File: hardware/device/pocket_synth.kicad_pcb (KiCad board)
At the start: 6 copper layers, 74 x 138 mm, 128 parts, among them IC2 IS42S16160J-7BLI, J1 POT_CONN, J10 HP_OUT, J2 USB, J3 MICRO_SD, J4 EXPANSION, J5 AUDIO_EXP, J8 LINE_OUT, J9 LINE_IN, SW1 TRIG1, SW10 TRIG10, SW11 TRIG11, SW12 TRIG12, SW13 TRIG13, SW14 TRIG14, SW15 TRIG15, SW16 TRIG16, SW17 KMR221NGLFS, SW18 HELP, SW2 TRIG2, SW3 TRIG3, SW4 TRIG4, SW5 TRIG5, SW6 TRIG6, SW7 TRIG7, SW8 TRIG8, SW9 TRIG9, U1 FSA2466UMX, U10 TRIG9, U11 TRIG13, U12 TRIG10, U13 TRIG14, U14 TRIG11, U15 TRIG15, U16 TRIG12, U17 TRIG16, U18 STM32H743ZIT6, U19 ER-TFT024IPS-3, U2 TRIG1, U20 TPS62A02DRL, U21 TPS560200, U22 MAX17261xxTD, U23 BQ21040DBV, U25 TCA8418RTWR, U26 FUSB303BTMX, U27 FUSB302B01MPX, U29 NAU88C22YG, U3 TRIG2, U4 TRIG3, U5 TRIG4, U6 TRIG8, U7 TRIG7, U8 TRIG6, U9 TRIG5

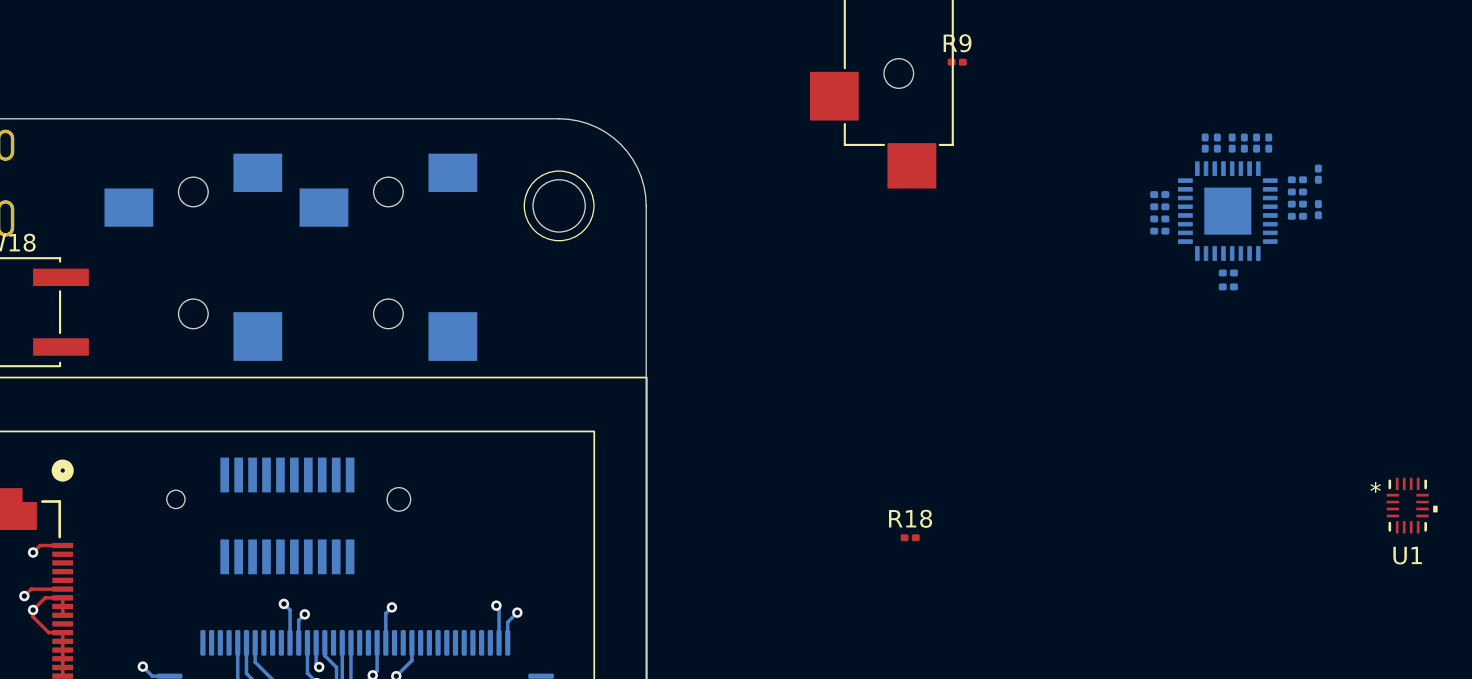
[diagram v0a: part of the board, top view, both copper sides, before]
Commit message: feat: add speaker
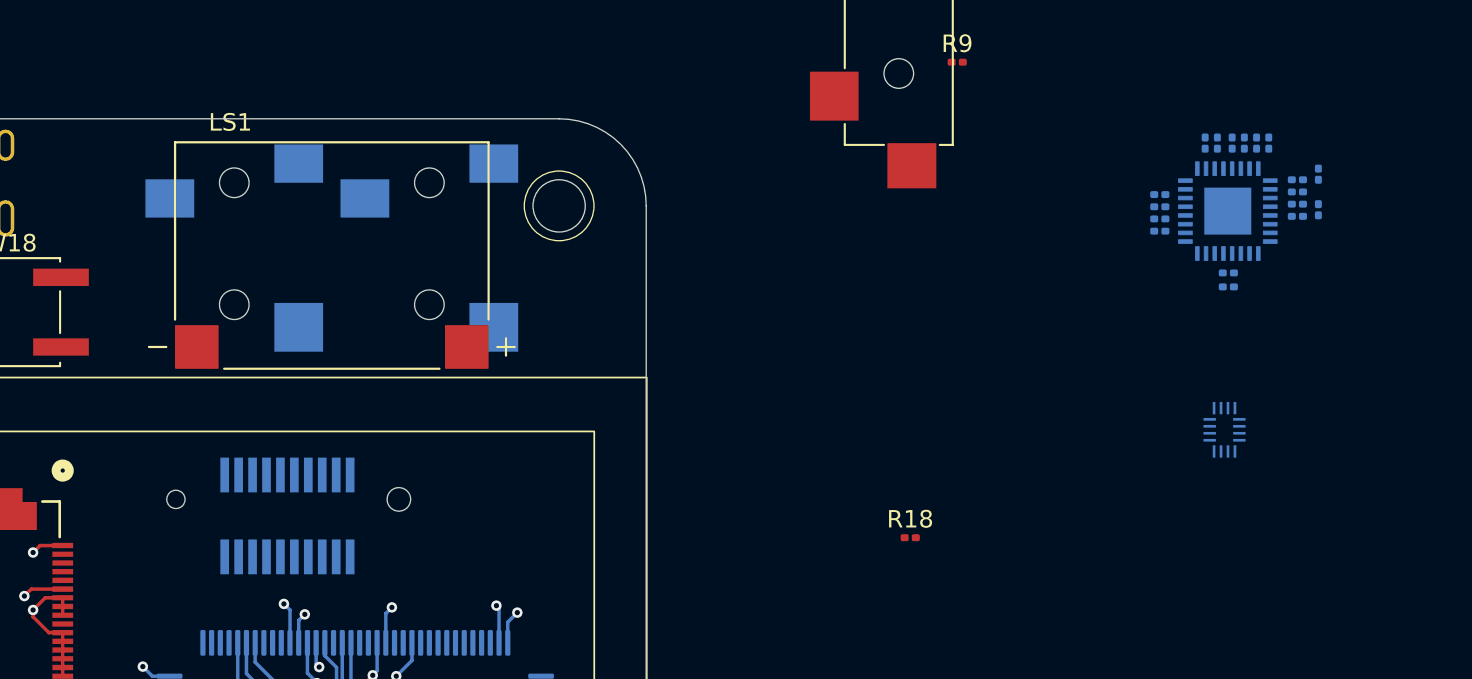
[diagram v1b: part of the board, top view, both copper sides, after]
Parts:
- added LS1: SPK, pocket_synth:AS01808AO-SC18-WP-R, F.Cu at (86.0, 37.9)
- U1: moved to B.Cu
- moved U1 11.4 mm to (137.2, 47.9), turned to 180 degrees
- moved J8 2.41 mm to (91.5, 36.2)
- moved J9 2.41 mm to (80.3, 36.2)

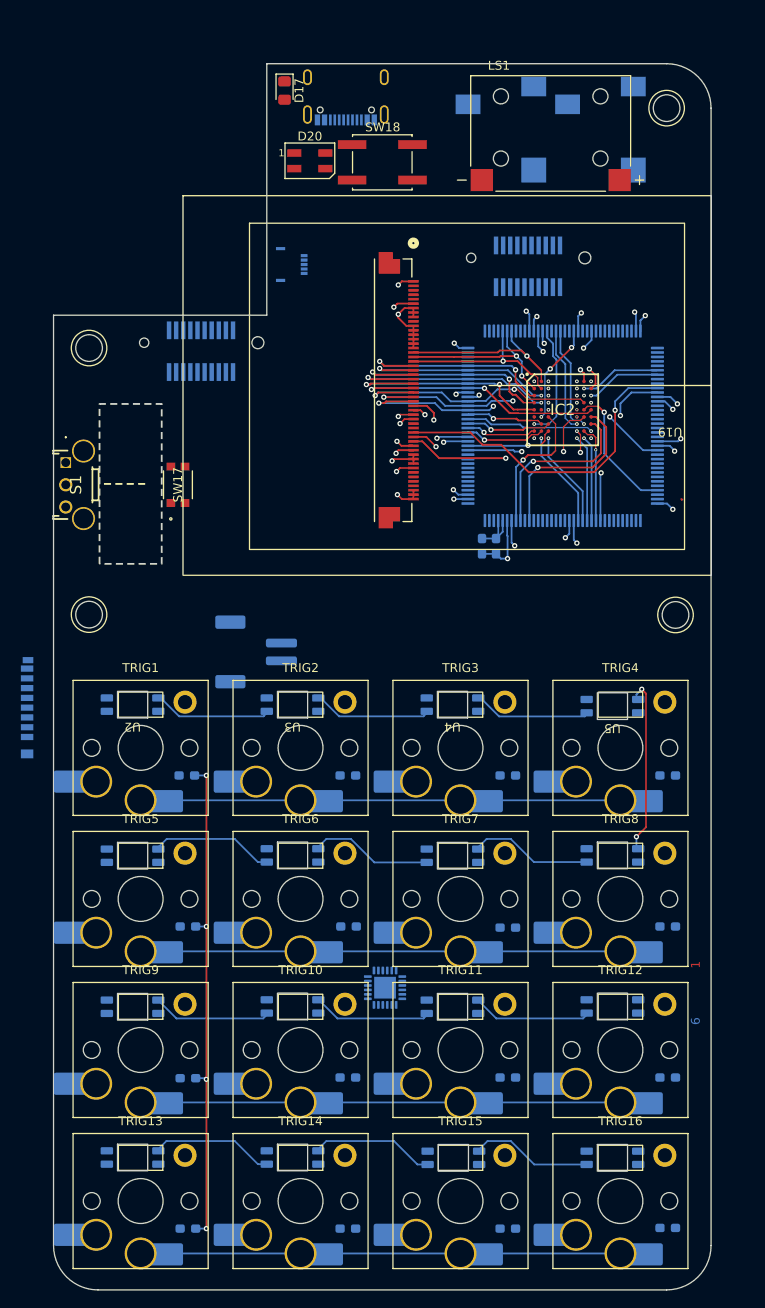
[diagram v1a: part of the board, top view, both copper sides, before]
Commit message: feat: add MEMs microphone
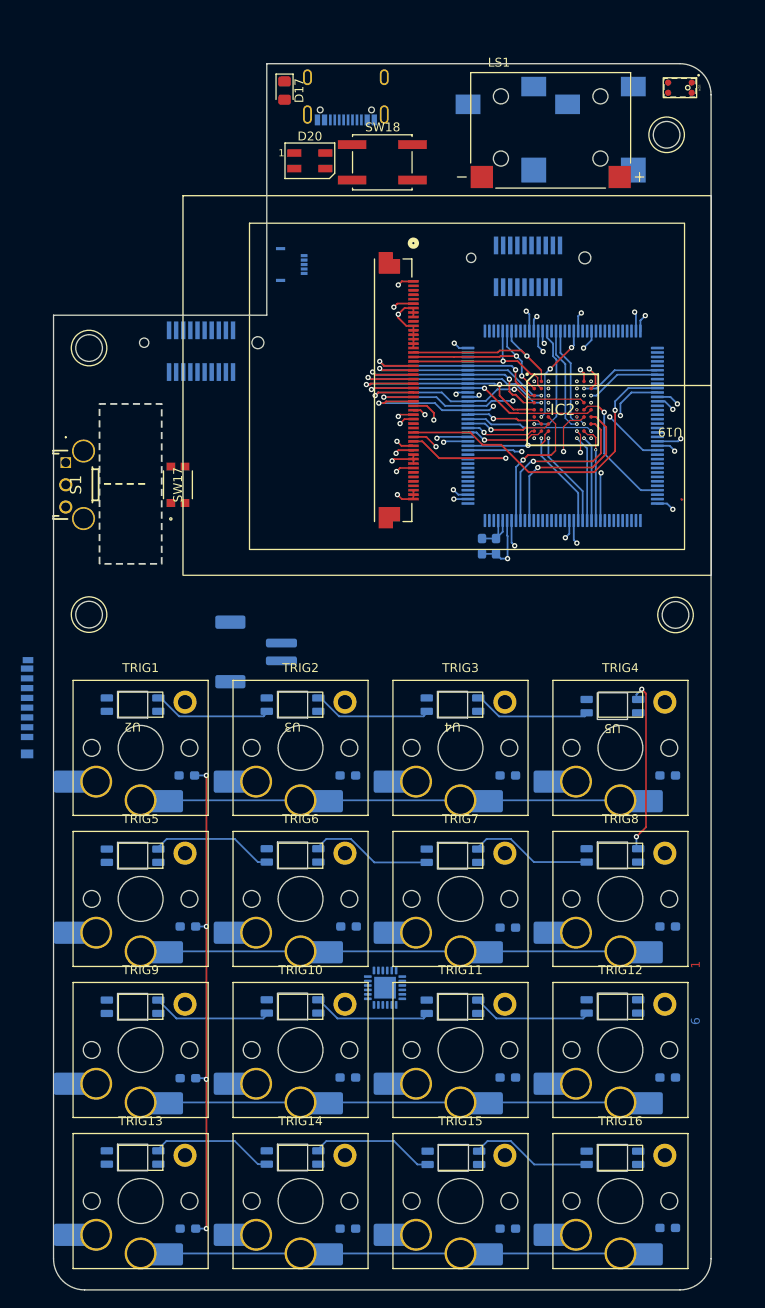
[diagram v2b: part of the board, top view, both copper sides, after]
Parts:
- added U24: MIC, pocket_synth:LMA3722T421-OA5, F.Cu at (100.5, 32.7)
- moved LS1 0.35 mm to (86.0, 37.5)
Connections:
- C32 pad 1: /Audio/LMICP -> Net-(C32-Pad1)
- C47 pad 1: /Audio/RMICP -> Net-(C47-Pad1)
- J9 pad R: Net-(U1-2A) -> Net-(C47-Pad1)
- J9 pad T: Net-(U1-1A) -> Net-(C32-Pad1)
- R19 pad 1: /Audio/LMICP -> Net-(C32-Pad1)
- R25 pad 1: /Audio/RMICP -> Net-(C47-Pad1)
- U1 pad 16: Net-(U1-1A) -> unconnected-(U1-1A-Pad16)
- U1 pad 4: Net-(U1-2A) -> unconnected-(U1-2A-Pad4)
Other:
- outline, holes or cut-outs redrawn
- board text added: "Case will have lanyard loop positioned in bottom center, under PCB."
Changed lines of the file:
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@@
 	(net 304 "Net-(C35-Pad2)")
 	(net 305 "Net-(C34-Pad2)")
-	(net 306 "Net-(U1-2A)")
-	(net 307 "Net-(U1-1A)")
+	(net 306 "Net-(C32-Pad1)")
+	(net 307 "Net-(C47-Pad1)")
 	(net 308 "Net-(C37-Pad2)")
 	(net 309 "/Audio/JACK_DET")
@@
 	(net 333 "Net-(U29-RSPKOUT)")
 	(net 334 "unconnected-(U29-RLIN{slash}GPIO3-Pad6)")
+	(net 335 "unconnected-(U1-2A-Pad4)")
+	(net 336 "unconnected-(U1-1A-Pad16)")
+	(net 337 "unconnected-(U24-OUT-Pad1)")
 	(footprint "pocket_synth:SW_Hotswap_Kailh_Choc_V1V2_Plated_1.00u"
 		(layer "F.Cu")
@@
 		)
 	)
+	(footprint "pocket_synth:LMA3722T421-OA5"
+		(layer "F.Cu")
+		(at 100.5 32.7 -90)
+		(property "Reference" "U24"
+			(at 0 -2.2 270)
+			(unlocked yes)
+			(layer "F.SilkS")
+			(effects
+				(font
+					(size 0.25 0.25)
+					(thickness 0.0625)
+				)
+			)
+		)
+		(property "Value" "MIC"
+			(at 0 2.3 270)
+			(unlocked yes)
+			(layer "F.Fab")
+			(effects
+				(font
+					(size 0.25 0.25)
+					(thickness 0.04)
+				)
+			)
+		)
+		(property "Datasheet" "https://jlcpcb.com/api/file/downloadByFileSystemAccessId/8603050779259248640"
+			(at 0 0 270)
+			(unlocked yes)
+			(layer "F.Fab")
+			(hide yes)
+			(effects
+				(font
+					(size 1 1)
+					(thickness 0.15)
+				)
+			)
+		)
+		(property "Description" "LMA3722T421-OA5"
+			(at 0 0 270)
+			(unlocked yes)
+			(layer "F.Fab")
+			(hide yes)
+			(effects
+				(font
+					(size 1 1)
+					(thickness 0.15)
+				)
+			)
+		)
+		(sheetname "/Audio/")
+		(sheetfile "audio.kicad_sch")
+		(attr smd)
+		(fp_rect
+			(start -1.05 -1.8)
+			(end 1.05 1.8)
+			(stroke
+				(width 0.05)
+				(type dash)
+			)
+			(fill no)
+			(layer "F.SilkS")
+		)
+		(fp_rect
+			(start -1.12 -1.88)
+			(end 1.12 1.88)
+			(stroke
+				(width 0.05)
+				(type solid)
+			)
+			(fill no)
+			(layer "F.SilkS")
+		)
+		(fp_circle
+			(center 0 -0.88)
+			(end 0.25 -0.88)
+			(stroke
+				(width 0.05)
+				(type solid)
+			)
+			(fill no)
+			(layer "F.SilkS")
+		)
+		(fp_circle
+			(center -1.4 -2.1)
+			(end -1.4 -2)
+			(stroke
+				(width 0.1)
+				(type solid)
+			)
+			(fill yes)
+			(layer "F.SilkS")
+		)
+		(fp_circle
+			(center -1.4 -2.1)
+			(end -1.4 -2)
+			(stroke
+				(width 0.1)
+				(type solid)
+			)
+			(fill yes)
+			(layer "F.Fab")
+		)
+		(fp_text user "${REFERENCE}"
+			(at 0 2.8 270)
+			(unlocked yes)
+			(layer "F.Fab")
+			(effects
+				(font
+					(size 0.25 0.25)
+					(thickness 0.04)
+				)
+			)
+		)
+		(pad "1" smd circle
+			(at -0.575 -1.33 270)
+			(size 0.7 0.7)
+			(layers "F.Cu" "F.Mask" "F.Paste")
+			(net 337 "unconnected-(U24-OUT-Pad1)")
+			(pinfunction "OUT")
+			(pintype "input")
+		)
+		(pad "2" smd circle
+			(at 0.575 -1.33 270)
+			(size 0.7 0.7)
+			(layers "F.Cu" "F.Mask" "F.Paste")
+			(net 51 "+3.3V")
+			(pinfunction "VDD")
+			(pintype "power_in")
+		)
+		(pad "3" smd circle
+			(at 0.575 1.33 270)
+			(size 0.7 0.7)
+			(layers "F.Cu" "F.Mask" "F.Paste")
+			(net 178 "GND")
+			(pinfunction "GND")
+			(pintype "power_out")
+		)
+		(pad "4" smd circle
+			(at -0.575 1.33 270)
+			(size 0.7 0.7)
+			(layers "F.Cu" "F.Mask" "F.Paste")
+			(net 178 "GND")
+			(pinfunction "GND")
+			(pintype "power_out")
+		)
+		(embedded_fonts no)
+	)
 	(footprint "pocket_synth:ER-TFT024IPS-3"
 		(layer "F.Cu")
@@
 	(footprint "pocket_synth:AS01808AO-SC18-WP-R"
 		(layer "F.Cu")
-		(at 85.95 37.85)
+		(at 85.95 37.5)
 		(property "Reference" "LS1"
 			(at -5.825 -7.635 0)
@@
 			)
 		)
-		(property "Description" ""
+		(property "Description" "AS01808AO-SC18-WP-R"
 			(at 0 0 0)
 			(layer "F.Fab")
@@
 			(size 2.8 2.2)
 			(layers "B.Cu" "B.Mask" "B.Paste")
-			(net 306 "Net-(U1-2A)")
+			(net 307 "Net-(C47-Pad1)")
 			(pintype "passive")
 		)
@@
 			(size 2.8 2.8)
 			(layers "B.Cu" "B.Mask" "B.Paste")
-			(net 307 "Net-(U1-1A)")
+			(net 306 "Net-(C32-Pad1)")
 			(pintype "passive")
 		)
@@
 			(layers "B.Cu" "B.Mask")
 			(roundrect_rratio 0.25)
-			(net 311 "/Audio/LMICP")
+			(net 306 "Net-(C32-Pad1)")
 			(pintype "passive")
 		)
@@
 			(layers "B.Cu" "B.Mask")
 			(roundrect_rratio 0.25)
-			(net 311 "/Audio/LMICP")
+			(net 306 "Net-(C32-Pad1)")
 			(pintype "passive")
 		)
@@
 			(layers "B.Cu" "B.Mask")
 			(roundrect_rratio 0.25)
-			(net 312 "/Audio/RMICP")
+			(net 307 "Net-(C47-Pad1)")
 			(pintype "passive")
 		)
@@
 			(layers "B.Cu" "B.Mask")
 			(roundrect_rratio 0.25)
-			(net 312 "/Audio/RMICP")
+			(net 307 "Net-(C47-Pad1)")
 			(pintype "passive")
 		)
@@
 			(size 0.1524 0.7112)
 			(layers "B.Cu" "B.Mask" "B.Paste")
-			(net 306 "Net-(U1-2A)")
+			(net 335 "unconnected-(U1-2A-Pad4)")
 			(pinfunction "2A")
 			(pintype "bidirectional")
@@
 			(size 0.1524 0.7112)
 			(layers "B.Cu" "B.Mask" "B.Paste")
-			(net 307 "Net-(U1-1A)")
+			(net 336 "unconnected-(U1-1A-Pad16)")
 			(pinfunction "1A")
 			(pintype "bidirectional")
@@
 	)
 	(gr_circle
-		(center 99 35)
-		(end 101 35)
+		(center 99 38)
+		(end 101 38)
 		(stroke
 			(width 0.05)
@@
 	)
 	(gr_line
-		(start 104 35)
-		(end 104 163)
+		(start 104 33.5)
+		(end 104 164.5)
 		(stroke
 			(width 0.05)
@@
 	)
 	(gr_line
-		(start 30 163)
+		(start 30 164.5)
 		(end 30 58.3)
 		(stroke
@@
 	)
 	(gr_arc
-		(start 104 163)
-		(mid 102.535534 166.535534)
-		(end 99 168)
+		(start 104 164.5)
+		(mid 102.974874 166.974874)
+		(end 100.5 168)
 		(stroke
 			(width 0.05)
@@
 	)
 	(gr_line
-		(start 99 168)
-		(end 35 168)
+		(start 100.5 168)
+		(end 33.5 168)
 		(stroke
 			(width 0.05)
@@
 	)
 	(gr_arc
-		(start 99 30)
-		(mid 102.535534 31.464466)
-		(end 104 35)
+		(start 100.5 30)
+		(mid 102.974874 31.025126)
+		(end 104 33.5)
 		(stroke
 			(width 0.05)
@@
 	)
 	(gr_arc
-		(start 35 168)
-		(mid 31.464466 166.535534)
-		(end 30 163)
+		(start 33.5 168)
+		(mid 31.025126 166.974874)
+		(end 30 164.5)
 		(stroke
 			(width 0.05)
@@
 	)
 	(gr_circle
-		(center 99 35)
-		(end 100.5 35)
+		(center 99 38)
+		(end 100.5 38)
 		(stroke
 			(width 0.05)
@@
 	(gr_line
 		(start 54 30)
-		(end 99 30)
+		(end 100.5 30)
 		(stroke
 			(width 0.05)
@@
 		)
 	)
+	(gr_text "Case will have lanyard loop positioned\nin bottom center, under PCB."
+		(at 67 170.6 0)
+		(layer "Cmts.User")
+		(effects
+			(font
+				(size 0.75 0.75)
+				(thickness 0.1)
+			)
+			(justify bottom)
+		)
+	)
 	(dimension
 		(type orthogonal)
-		(layer "F.SilkS")
+		(layer "Dwgs.User")
 		(pts
-			(xy 99 168) (xy 95.8 30)
+			(xy 104 163) (xy 30 163)
 		)
-		(height 13)
-		(orientation 1)
+		(height 13.1)
+		(orientation 0)
 		(format
 			(prefix "")
@@
 		)
 		(style
-			(thickness 0.1)
+			(thickness 0.05)
 			(arrow_length 1.27)
 			(text_position_mode 0)
@@
 			(keep_text_aligned yes)
 		)
-		(gr_text "138"
-			(at 110.9 99 90)
-			(layer "F.SilkS")
+		(gr_text "74"
+			(at 67 174.95 0)
+			(layer "Dwgs.User")
 			(effects
 				(font
 					(size 1 1)
-					(thickness 0.1)
+					(thickness 0.15)
 				)
 			)
@@
 		(layer "Dwgs.User")
 		(pts
-			(xy 104 163) (xy 30 163)
+			(xy 99 168) (xy 95.8 30)
 		)
-		(height 10)
-		(orientation 0)
+		(height 13)
+		(orientation 1)
 		(format
 			(prefix "")
@@
 		)
 		(style
-			(thickness 0.05)
+			(thickness 0.1)
 			(arrow_length 1.27)
 			(text_position_mode 0)
@@
 			(keep_text_aligned yes)
 		)
-		(gr_text "74"
-			(at 67 171.85 0)
+		(gr_text "138"
+			(at 110.9 99 90)
 			(layer "Dwgs.User")
 			(effects
 				(font
 					(size 1 1)
-					(thickness 0.15)
+					(thickness 0.1)
 				)
 			)
